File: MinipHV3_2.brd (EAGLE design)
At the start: 27.9 x 27.9 mm, 37 parts, among them IC1 MCP3221, IC4 LMP7702, IC5 TPS60400DBV

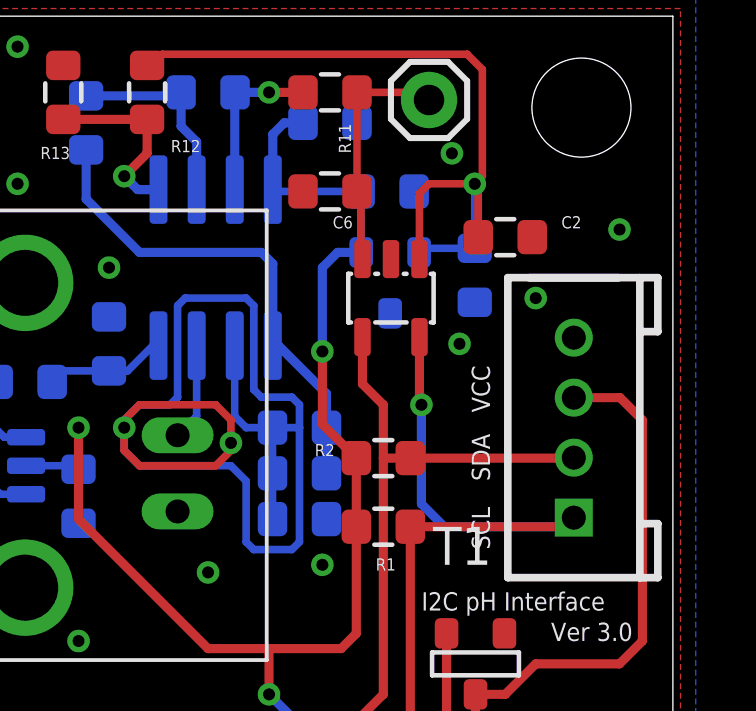
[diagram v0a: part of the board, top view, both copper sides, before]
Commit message: added in bridge jumper VCC to Vref
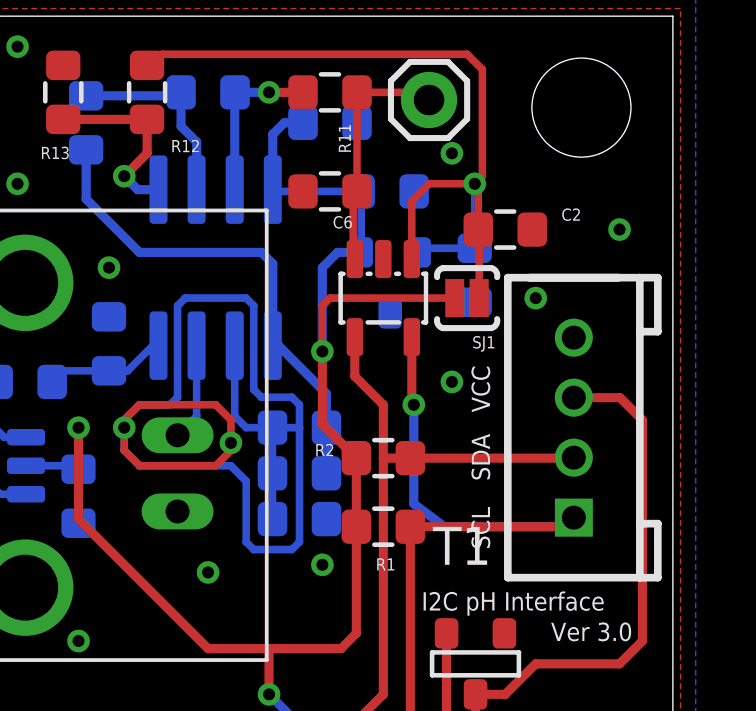
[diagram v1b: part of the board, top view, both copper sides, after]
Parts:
- added SJ1: SOLDERJUMPERNC2, SparkFun:SJ_2S-NOTRACE
- moved IC1 0.25 mm to (18.3, 18.5)
- moved C2 0.25 mm to (22.4, 20.8)
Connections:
- net +5V: now also SJ1.2
- net VREF: now also SJ1.1
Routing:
- net +5V: track 50.5 -> 56.6 mm
- net VREF: track 25.5 -> 27.7 mm
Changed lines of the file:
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@@
 </autorouter>
 <elements>
-<element name="IC1" library="SparkysWidgets" package="SOT23-DBV" value="MCP3221" x="18.542" y="18.542" smashed="yes" rot="R180">
-<attribute name="VALUE" x="19.685" y="18.669" size="0.4064" layer="27" rot="R180"/>
+<element name="IC1" library="SparkysWidgets" package="SOT23-DBV" value="MCP3221" x="18.288" y="18.542" smashed="yes" rot="R180">
+<attribute name="VALUE" x="19.431" y="18.669" size="0.4064" layer="27" rot="R180"/>
 </element>
 <element name="U$2" library="SparkysWidgets" package="BNC" value="BNCPTH" x="11.43" y="13.97" smashed="yes" rot="R90"/>
@@
 <attribute name="VALUE" x="22.098" y="21.209" size="0.4064" layer="28" rot="MR0"/>
 </element>
-<element name="C2" library="SparkysWidgets" package="0805" value=".1uF" x="22.352" y="20.574" smashed="yes" rot="R180">
-<attribute name="NAME" x="24.892" y="21.2725" size="0.4064" layer="25" rot="R180"/>
-<attribute name="VALUE" x="25.146" y="20.447" size="0.4064" layer="27" rot="R180"/>
+<element name="C2" library="SparkysWidgets" package="0805" value=".1uF" x="22.352" y="20.828" smashed="yes" rot="R180">
+<attribute name="NAME" x="24.892" y="21.5265" size="0.4064" layer="25" rot="R180"/>
+<attribute name="VALUE" x="25.146" y="20.701" size="0.4064" layer="27" rot="R180"/>
 </element>
 <element name="R1" library="SparkysWidgets" package="0805" value="3K" x="18.288" y="10.922" smashed="yes" rot="R180">
@@
 <element name="C7" library="SparkysWidgets" package="0805" value=".1uF" x="9.144" y="17.018" rot="MR270"/>
 <element name="T1" library="SparkysWidgets" package="SOT-23" value="" x="21.336" y="6.35"/>
+<element name="SJ1" library="SparkFun" package="SJ_2S-NOTRACE" value="SOLDERJUMPERNC2" x="21.082" y="18.542" rot="R180"/>
 </elements>
 <signals>
@@
 <via x="14.478" y="5.334" extent="1-16" drill="0.4"/>
 <wire x1="14.478" y1="5.334" x2="14.478" y2="6.858" width="0.3048" layer="1"/>
+<contactref element="SJ1" pad="2"/>
+<wire x1="16.256" y1="16.764" x2="16.256" y2="18.288" width="0.254" layer="1"/>
+<wire x1="16.256" y1="18.288" x2="16.51" y2="18.542" width="0.254" layer="1"/>
+<wire x1="16.51" y1="18.542" x2="20.6693" y2="18.542" width="0.254" layer="1"/>
 </signal>
 <signal name="N$1">
@@
 <via x="23.368" y="18.542" extent="1-16" drill="0.4"/>
 <via x="20.574" y="23.368" extent="1-16" drill="0.4"/>
-<via x="20.828" y="17.018" extent="1-16" drill="0.4"/>
+<via x="20.574" y="15.748" extent="1-16" drill="0.4"/>
 <via x="21.59" y="1.27" extent="1-16" drill="0.4"/>
 <via x="6.096" y="26.924" extent="1-16" drill="0.4"/>
@@
 <contactref element="IC1" pad="3"/>
 <contactref element="C6" pad="1"/>
-<wire x1="17.537" y1="19.897" x2="17.592" y2="19.842" width="0.254" layer="1"/>
-<wire x1="17.537" y1="19.897" x2="17.537" y2="21.971" width="0.254" layer="1"/>
-<wire x1="17.537" y1="21.971" x2="17.41" y2="22.098" width="0.254" layer="1"/>
+<wire x1="17.283" y1="20.151" x2="17.338" y2="19.842" width="0.254" layer="1"/>
+<wire x1="17.283" y1="20.151" x2="17.283" y2="22.225" width="0.254" layer="1"/>
+<wire x1="17.283" y1="22.225" x2="17.41" y2="22.098" width="0.254" layer="1"/>
 <wire x1="17.41" y1="22.098" x2="17.41" y2="25.4" width="0.254" layer="1"/>
 <wire x1="19.812" y1="25.146" x2="19.558" y2="25.4" width="0.254" layer="1"/>
@@
 <wire x1="24.638" y1="11.176" x2="24.384" y2="10.922" width="0.3048" layer="16"/>
 <wire x1="24.384" y1="10.922" x2="20.32" y2="10.922" width="0.3048" layer="16"/>
-<wire x1="20.32" y1="10.922" x2="19.558" y2="11.684" width="0.3048" layer="16"/>
-<wire x1="19.558" y1="11.684" x2="19.558" y2="14.986" width="0.3048" layer="16"/>
-<via x="19.558" y="14.986" extent="1-16" drill="0.4"/>
-<wire x1="19.558" y1="14.986" x2="19.558" y2="15.24" width="0.3048" layer="1"/>
-<wire x1="19.492" y1="17.242" x2="19.492" y2="15.306" width="0.3048" layer="1"/>
-<wire x1="19.492" y1="15.306" x2="19.558" y2="15.24" width="0.3048" layer="1"/>
+<wire x1="20.32" y1="10.922" x2="19.304" y2="11.684" width="0.3048" layer="16"/>
+<wire x1="19.304" y1="11.684" x2="19.304" y2="14.986" width="0.3048" layer="16"/>
+<via x="19.304" y="14.986" extent="1-16" drill="0.4"/>
+<wire x1="19.238" y1="17.242" x2="19.238" y2="15.052" width="0.3048" layer="1"/>
+<wire x1="19.238" y1="15.052" x2="19.304" y2="14.986" width="0.3048" layer="1"/>
 </signal>
 <signal name="SDA">
@@
 <wire x1="18.288" y1="5.334" x2="18.288" y2="13.208" width="0.3048" layer="1"/>
 <wire x1="18.288" y1="13.208" x2="18.288" y2="14.986" width="0.3048" layer="1"/>
-<wire x1="18.288" y1="14.986" x2="17.592" y2="15.682" width="0.3048" layer="1"/>
-<wire x1="17.592" y1="17.242" x2="17.592" y2="15.682" width="0.3048" layer="1"/>
+<wire x1="18.288" y1="14.986" x2="17.338" y2="15.936" width="0.3048" layer="1"/>
+<wire x1="17.338" y1="17.242" x2="17.338" y2="15.936" width="0.3048" layer="1"/>
 <wire x1="19.188" y1="13.208" x2="18.288" y2="13.208" width="0.3048" layer="1"/>
 </signal>
@@
 <contactref element="C2" pad="2"/>
 <contactref element="R12" pad="1"/>
-<wire x1="21.452" y1="20.574" x2="21.452" y2="22.236" width="0.254" layer="1"/>
+<wire x1="21.452" y1="20.828" x2="21.452" y2="22.236" width="0.254" layer="1"/>
 <wire x1="21.452" y1="22.236" x2="21.336" y2="22.352" width="0.254" layer="1"/>
 <via x="21.336" y="22.352" extent="1-16" drill="0.4"/>
@@
 <wire x1="21.336" y1="20.204" x2="19.6198" y2="20.204" width="0.254" layer="16"/>
 <wire x1="19.6198" y1="20.204" x2="19.4818" y2="20.066" width="0.254" layer="16"/>
-<wire x1="19.492" y1="19.842" x2="19.492" y2="22.032" width="0.254" layer="1"/>
-<wire x1="19.492" y1="22.032" x2="19.812" y2="22.352" width="0.254" layer="1"/>
+<wire x1="19.238" y1="19.842" x2="19.238" y2="21.778" width="0.254" layer="1"/>
+<wire x1="19.238" y1="21.778" x2="19.812" y2="22.352" width="0.254" layer="1"/>
 <wire x1="19.812" y1="22.352" x2="21.336" y2="22.352" width="0.254" layer="1"/>
 <wire x1="10.414" y1="26.3" x2="10.552" y2="26.3" width="0.254" layer="1"/>
@@
 <wire x1="21.59" y1="26.162" x2="21.59" y2="22.606" width="0.254" layer="1"/>
 <wire x1="21.59" y1="22.606" x2="21.336" y2="22.352" width="0.254" layer="1"/>
+<contactref element="SJ1" pad="1"/>
+<wire x1="21.4829" y1="18.542" x2="21.4829" y2="20.7971" width="0.254" layer="1"/>
+<wire x1="21.4829" y1="20.7971" x2="21.452" y2="20.828" width="0.254" layer="1"/>
 </signal>
 <signal name="N$4">
